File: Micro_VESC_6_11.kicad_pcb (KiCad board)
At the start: 4 copper layers, 34 x 44.5 mm, 208 parts, among them J1 Motor_Conn, J2 CONN_01X01, J3 CONN_01X01, J4 CONN_01X01, J5 CONN_01X01, J6 CONN_01X01, J7 SWD, J8 COMM_1, J9 COMM_2, Q1 NTMFS5C604NLT1G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

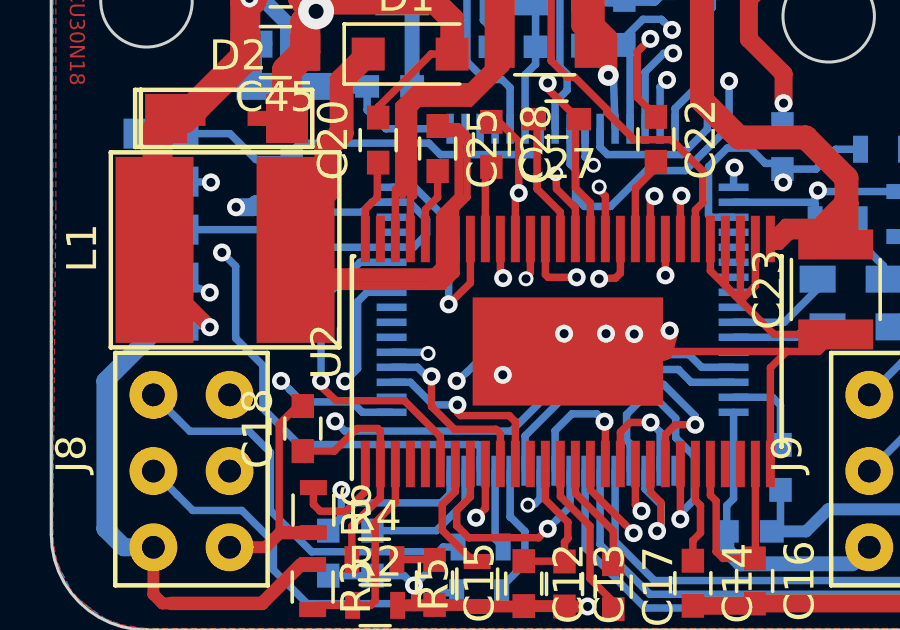
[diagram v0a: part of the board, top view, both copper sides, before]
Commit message: Add files via upload
Updated the kicad_pcb file: corrected some track placements.
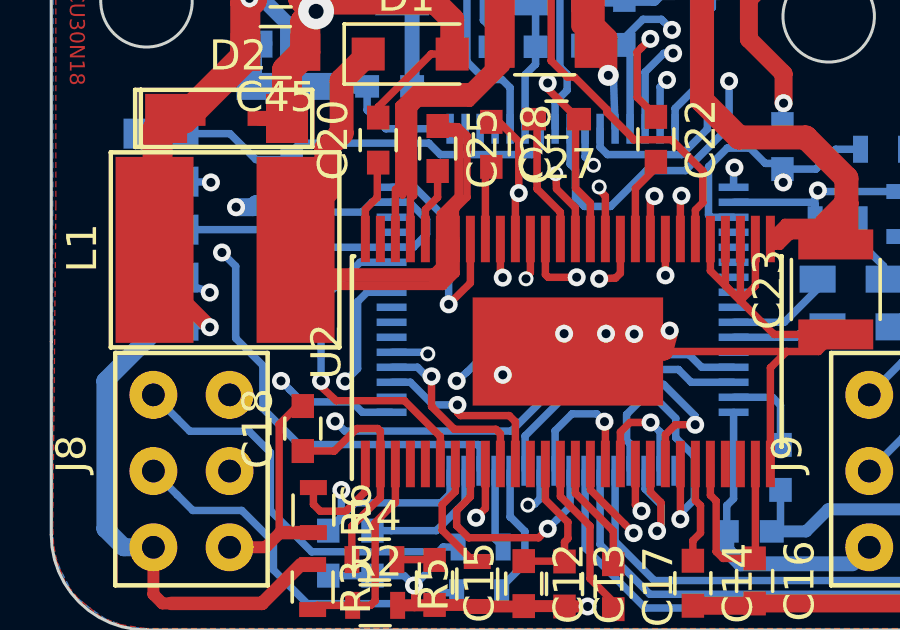
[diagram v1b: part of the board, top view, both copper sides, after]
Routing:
- net GNDPWR: track 286.9 -> 288.1 mm
